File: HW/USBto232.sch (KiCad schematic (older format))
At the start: 17 parts

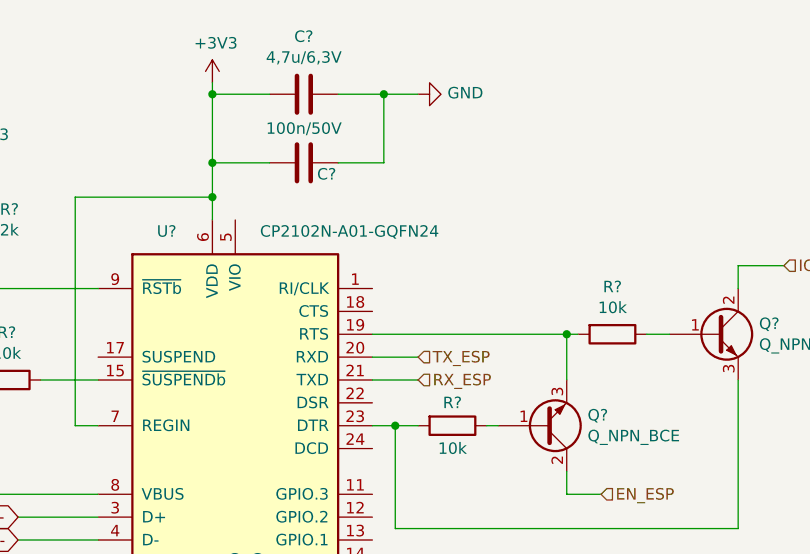
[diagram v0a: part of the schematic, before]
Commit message: add power supply for ESP, erase resistors by buttons, add power supply for CP2102, add communication control (CP2102-ESP)
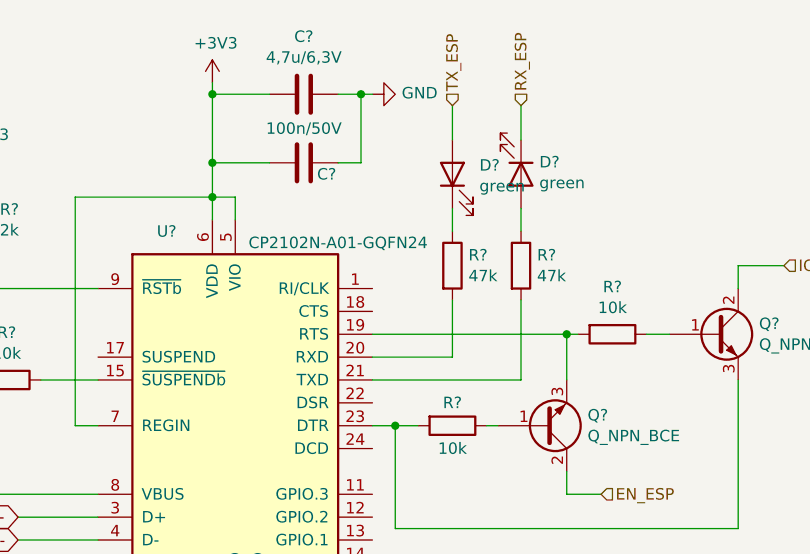
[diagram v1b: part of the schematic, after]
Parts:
- added D? (x2): green, symbol Device:LED
- added R? (x2): 47k, symbol Device:R
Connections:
- net +3V3: now also U?.5 (VIO)
- net RX_ESP: now also D?.1 (K); no longer U?.21 (TXD)
- net TX_ESP: now also D?.2 (A); no longer U?.20 (RXD)
- new net: D?.1 (K), R?.1
- new net: R?.2, U?.20 (RXD)
- new net: D?.2 (A), R?.1
- new net: R?.2, U?.21 (TXD)
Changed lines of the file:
@@
 $Descr A4 11693 8268
 encoding utf-8
-Sheet 6 9
+Sheet 13 16
 Title ""
 Date ""
@@
 Comment4 ""
 $EndDescr
-Wire Wire Line
-	6150 2800 6350 2800
-Wire Wire Line
-	6350 2900 6150 2900
 $Comp
 L Connector:USB_B_Micro J?
@@
 	1    0    0    -1
 $EndComp
-Text HLabel 6350 2800 2    50   Input ~ 0
+Text HLabel 6500 1700 1    50   Input ~ 0
 TX_ESP
-Text HLabel 6350 2900 2    50   Input ~ 0
+Text HLabel 6800 1700 1    50   Input ~ 0
 RX_ESP
 $Comp
@@
 	5450 1950 5450 2100
 Wire Wire Line
-	6000 1650 6200 1650
-Wire Wire Line
-	6200 1650 6200 1950
-Wire Wire Line
-	6200 1950 6000 1950
+	6000 1650 6100 1650
+Wire Wire Line
+	6100 1650 6100 1950
+Wire Wire Line
+	6100 1950 6000 1950
 $Comp
 L power:GND #PWR?
 U 1 1 5FBD8F58
-P 6350 1650
-F 0 "#PWR?" H 6350 1400 50  0001 C CNN
-F 1 "GND" V 6355 1522 50  0000 R CNN
-F 2 "" H 6350 1650 50  0001 C CNN
-F 3 "" H 6350 1650 50  0001 C CNN
-	1    6350 1650
+P 6150 1650
+F 0 "#PWR?" H 6150 1400 50  0001 C CNN
+F 1 "GND" V 6155 1522 50  0000 R CNN
+F 2 "" H 6150 1650 50  0001 C CNN
+F 3 "" H 6150 1650 50  0001 C CNN
+	1    6150 1650
 	0    -1   -1   0
 $EndComp
 Wire Wire Line
-	6350 1650 6200 1650
-Connection ~ 6200 1650
+	6150 1650 6100 1650
+Connection ~ 6100 1650
 $Comp
 L Device:R R?
@@
 AR Path="/5FBB3550/5FBB605D" Ref="U?"  Part="1"
 F 0 "U?" H 5250 3950 50  0000 C CNN
-F 1 "CP2102N-A01-GQFN24" H 6050 3950 50  0000 C CNN
+F 1 "CP2102N-A01-GQFN24" H 6000 3900 50  0000 C CNN
 F 2 "Package_DFN_QFN:QFN-24-1EP_4x4mm_P0.5mm_EP2.6x2.6mm" H 6000 2300 50  0001 L CNN
 F 3 "https://www.silabs.com/documents/public/data-sheets/cp2102n-datasheet.pdf" H 5600 2050 50  0001 C CNN
@@
 $EndComp
 NoConn ~ 1600 3050
+Wire Wire Line
+	5550 2200 5550 2100
+Wire Wire Line
+	5550 2100 5450 2100
+$Comp
+L Device:R R?
+U 1 1 5F7740AD
+P 6500 2400
+F 0 "R?" H 6570 2446 50  0000 L CNN
+F 1 "47k" H 6570 2355 50  0000 L CNN
+F 2 "" V 6430 2400 50  0001 C CNN
+F 3 "~" H 6500 2400 50  0001 C CNN
+	1    6500 2400
+	1    0    0    -1
+$EndComp
+$Comp
+L Device:R R?
+U 1 1 5F774323
+P 6800 2400
+F 0 "R?" H 6870 2446 50  0000 L CNN
+F 1 "47k" H 6870 2355 50  0000 L CNN
+F 2 "" V 6730 2400 50  0001 C CNN
+F 3 "~" H 6800 2400 50  0001 C CNN
+	1    6800 2400
+	1    0    0    -1
+$EndComp
+$Comp
+L Device:LED D?
+U 1 1 5F774688
+P 6500 2000
+F 0 "D?" V 6539 1882 50  0000 R CNN
+F 1 "green" V 6448 1882 50  0000 R CNN
+F 2 "" H 6500 2000 50  0001 C CNN
+F 3 "~" H 6500 2000 50  0001 C CNN
+	1    6500 2000
+	0    -1   -1   0
+$EndComp
+$Comp
+L Device:LED D?
+U 1 1 5F774C1B
+P 6800 2000
+F 0 "D?" V 6747 2080 50  0000 L CNN
+F 1 "green" V 6838 2080 50  0000 L CNN
+F 2 "" H 6800 2000 50  0001 C CNN
+F 3 "~" H 6800 2000 50  0001 C CNN
+	1    6800 2000
+	0    1    1    0
+$EndComp
+Wire Wire Line
+	6500 1700 6500 1850
+Wire Wire Line
+	6800 1700 6800 1850
+Wire Wire Line
+	6500 2150 6500 2250
+Wire Wire Line
+	6800 2150 6800 2250
+Wire Wire Line
+	6500 2550 6500 2800
+Wire Wire Line
+	6150 2800 6500 2800
+Wire Wire Line
+	6800 2900 6800 2550
+Wire Wire Line
+	6150 2900 6800 2900
 $EndSCHEMATC

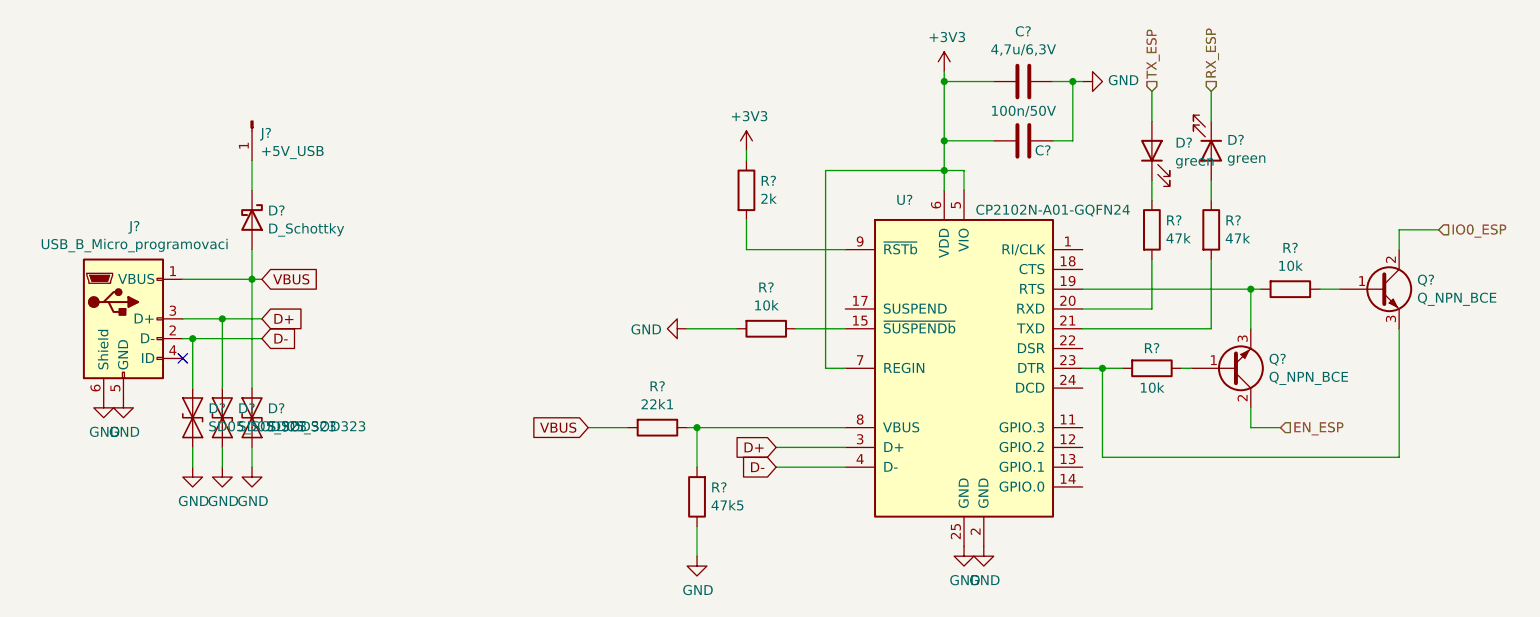
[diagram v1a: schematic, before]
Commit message: change USB
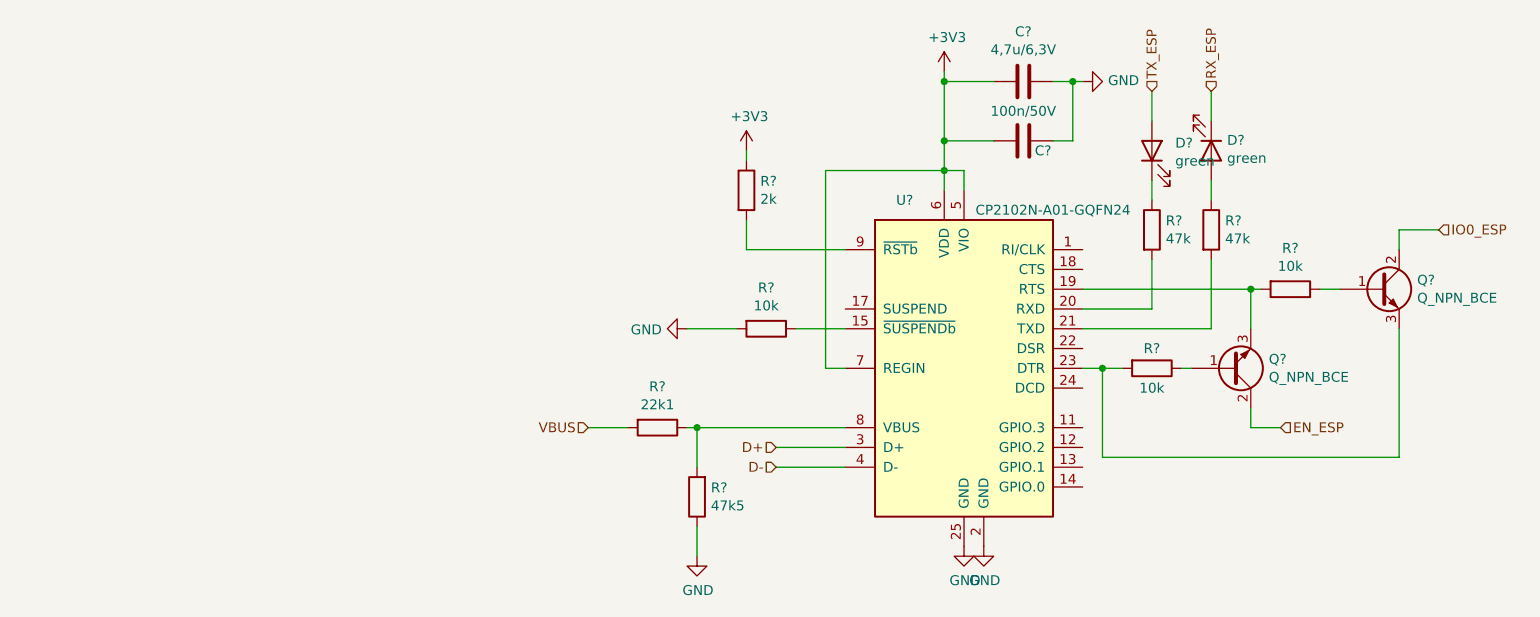
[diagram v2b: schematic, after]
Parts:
- removed D? (x3): SD05_SOD323, Diode_SMD:D_SOD-323, symbol Diode:SD05_SOD323
- removed D?: D_Schottky, symbol Device:D_Schottky
- removed J?: USB_B_Micro_programovaci, symbol Connector:USB_B_Micro
- removed J?: +5V_USB, symbol Connector:Conn_01x01_Male
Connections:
- no-connect marks 1 -> 0
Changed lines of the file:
@@
 $Descr A4 11693 8268
 encoding utf-8
-Sheet 13 16
+Sheet 13 17
 Title ""
 Date ""
@@
 Comment4 ""
 $EndDescr
-$Comp
-L Connector:USB_B_Micro J?
-U 1 1 5FBB6065
-P 1300 2850
-AR Path="/5FBB6065" Ref="J?"  Part="1"
-AR Path="/5FBB3550/5FBB6065" Ref="J?"  Part="1"
-F 0 "J?" H 1357 3317 50  0000 C CNN
-F 1 "USB_B_Micro_programovaci" H 1357 3226 50  0000 C CNN
-F 2 "" H 1450 2800 50  0001 C CNN
-F 3 "~" H 1450 2800 50  0001 C CNN
-	1    1300 2850
-	1    0    0    -1
-$EndComp
 Text HLabel 6500 1700 1    50   Input ~ 0
 TX_ESP
 Text HLabel 6800 1700 1    50   Input ~ 0
 RX_ESP
-$Comp
-L power:GND #PWR?
-U 1 1 5FBB7F58
-P 1300 3250
-F 0 "#PWR?" H 1300 3000 50  0001 C CNN
-F 1 "GND" H 1305 3077 50  0000 C CNN
-F 2 "" H 1300 3250 50  0001 C CNN
-F 3 "" H 1300 3250 50  0001 C CNN
-	1    1300 3250
-	1    0    0    -1
-$EndComp
 $Comp
 L power:GND #PWR?
@@
 Text HLabel 7950 2400 2    50   Input ~ 0
 IO0_ESP
-Text GLabel 4600 3500 0    50   Input ~ 0
-D+
-Text GLabel 4600 3600 0    50   Input ~ 0
-D-
-Text GLabel 2000 2850 2    50   Input ~ 0
-D+
-Text GLabel 2000 2950 2    50   Input ~ 0
-D-
-Wire Wire Line
-	2000 2850 1800 2850
-Wire Wire Line
-	1600 2950 1650 2950
 Wire Wire Line
 	4450 2500 4950 2500
@@
 Wire Wire Line
 	4200 3900 4200 4050
-Text GLabel 3650 3400 0    50   Input ~ 0
-VBUS
-Text GLabel 2000 2650 2    50   Input ~ 0
-VBUS
-Wire Wire Line
-	1600 2650 1950 2650
 $Comp
 L Interface_USB:CP2102N-A01-GQFN24 U?
@@
 	1    0    0    -1
 $EndComp
-$Comp
-L Diode:SD05_SOD323 D?
-U 1 1 5FBE6FA9
-P 1650 3350
-F 0 "D?" V 1696 3271 50  0000 R CNN
-F 1 "SD05_SOD323" V 1605 3271 50  0000 R CNN
-F 2 "Diode_SMD:D_SOD-323" H 1650 3150 50  0001 C CNN
-F 3 "https://www.littelfuse.com/~/media/electronics/datasheets/tvs_diode_arrays/littelfuse_tvs_diode_array_sd_c_datasheet.pdf.pdf" H 1650 3350 50  0001 C CNN
-	1    1650 3350
-	0    -1   -1   0
-$EndComp
 Wire Wire Line
 	4600 3500 4950 3500
 Wire Wire Line
 	4600 3600 4950 3600
-$Comp
-L Diode:SD05_SOD323 D?
-U 1 1 5FBE7A9C
-P 1800 3350
-F 0 "D?" V 1846 3271 50  0000 R CNN
-F 1 "SD05_SOD323" V 1755 3271 50  0000 R CNN
-F 2 "Diode_SMD:D_SOD-323" H 1800 3150 50  0001 C CNN
-F 3 "https://www.littelfuse.com/~/media/electronics/datasheets/tvs_diode_arrays/littelfuse_tvs_diode_array_sd_c_datasheet.pdf.pdf" H 1800 3350 50  0001 C CNN
-	1    1800 3350
-	0    -1   -1   0
-$EndComp
-$Comp
-L Diode:SD05_SOD323 D?
-U 1 1 5FBE7EF8
-P 1950 3350
-F 0 "D?" V 1996 3271 50  0000 R CNN
-F 1 "SD05_SOD323" V 1905 3271 50  0000 R CNN
-F 2 "Diode_SMD:D_SOD-323" H 1950 3150 50  0001 C CNN
-F 3 "https://www.littelfuse.com/~/media/electronics/datasheets/tvs_diode_arrays/littelfuse_tvs_diode_array_sd_c_datasheet.pdf.pdf" H 1950 3350 50  0001 C CNN
-	1    1950 3350
-	0    -1   -1   0
-$EndComp
-$Comp
-L power:GND #PWR?
-U 1 1 5FBE85DE
-P 1650 3600
-F 0 "#PWR?" H 1650 3350 50  0001 C CNN
-F 1 "GND" H 1655 3427 50  0000 C CNN
-F 2 "" H 1650 3600 50  0001 C CNN
-F 3 "" H 1650 3600 50  0001 C CNN
-	1    1650 3600
-	1    0    0    -1
-$EndComp
-$Comp
-L power:GND #PWR?
-U 1 1 5FBE8A8A
-P 1800 3600
-F 0 "#PWR?" H 1800 3350 50  0001 C CNN
-F 1 "GND" H 1805 3427 50  0000 C CNN
-F 2 "" H 1800 3600 50  0001 C CNN
-F 3 "" H 1800 3600 50  0001 C CNN
-	1    1800 3600
-	1    0    0    -1
-$EndComp
-$Comp
-L power:GND #PWR?
-U 1 1 5FBE8C03
-P 1950 3600
-F 0 "#PWR?" H 1950 3350 50  0001 C CNN
-F 1 "GND" H 1955 3427 50  0000 C CNN
-F 2 "" H 1950 3600 50  0001 C CNN
-F 3 "" H 1950 3600 50  0001 C CNN
-	1    1950 3600
-	1    0    0    -1
-$EndComp
-Wire Wire Line
-	1650 3500 1650 3600
-Wire Wire Line
-	1800 3500 1800 3600
-Wire Wire Line
-	1950 3500 1950 3600
-Wire Wire Line
-	1650 3200 1650 2950
-Connection ~ 1650 2950
-Wire Wire Line
-	1950 3200 1950 2650
-Connection ~ 1950 2650
-Wire Wire Line
-	1950 2650 2000 2650
-Wire Wire Line
-	1650 2950 2000 2950
-Wire Wire Line
-	1800 3200 1800 2850
-Connection ~ 1800 2850
-Wire Wire Line
-	1800 2850 1600 2850
-$Comp
-L Device:D_Schottky D?
-U 1 1 5FBF0650
-P 1950 2350
-F 0 "D?" V 1904 2430 50  0000 L CNN
-F 1 "D_Schottky" V 1995 2430 50  0000 L CNN
-F 2 "" H 1950 2350 50  0001 C CNN
-F 3 "~" H 1950 2350 50  0001 C CNN
-	1    1950 2350
-	0    1    1    0
-$EndComp
-Wire Wire Line
-	1950 2500 1950 2650
-$Comp
-L Connector:Conn_01x01_Male J?
-U 1 1 5FBF4956
-P 1950 1850
-F 0 "J?" V 2012 1894 50  0000 L CNN
-F 1 "+5V_USB" V 2103 1894 50  0000 L CNN
-F 2 "" H 1950 1850 50  0001 C CNN
-F 3 "~" H 1950 1850 50  0001 C CNN
-	1    1950 1850
-	0    1    1    0
-$EndComp
-Wire Wire Line
-	1950 2050 1950 2200
 Wire Wire Line
 	6650 3100 6700 3100
@@
 Wire Wire Line
 	3650 3400 3850 3400
-$Comp
-L power:GND #PWR?
-U 1 1 5F7442FA
-P 1200 3250
-F 0 "#PWR?" H 1200 3000 50  0001 C CNN
-F 1 "GND" H 1205 3077 50  0000 C CNN
-F 2 "" H 1200 3250 50  0001 C CNN
-F 3 "" H 1200 3250 50  0001 C CNN
-	1    1200 3250
-	1    0    0    -1
-$EndComp
-NoConn ~ 1600 3050
 Wire Wire Line
 	5550 2200 5550 2100
@@
 Wire Wire Line
 	6150 2900 6800 2900
+Text HLabel 3650 3400 0    50   Input ~ 0
+VBUS
+Text HLabel 4600 3500 0    50   Input ~ 0
+D+
+Text HLabel 4600 3600 0    50   Input ~ 0
+D-
 $EndSCHEMATC

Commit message: add some packages
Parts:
- C?: footprint (none) -> Capacitor_SMD:C_1206_3216Metric
- D? (x2): footprint (none) -> LED_SMD:LED_0603_1608Metric
- Q? (x2): footprint (none) -> Package_TO_SOT_SMD:SOT-23
- R? (x2): footprint (none) -> Resistor_SMD:R_0402_1005Metric
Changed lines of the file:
@@
 F 0 "Q?" H 7841 2746 50  0000 L CNN
 F 1 "Q_NPN_BCE" H 7841 2655 50  0000 L CNN
-F 2 "" H 7850 2800 50  0001 C CNN
+F 2 "Package_TO_SOT_SMD:SOT-23" H 7850 2800 50  0001 C CNN
 F 3 "~" H 7650 2700 50  0001 C CNN
 	1    7650 2700
@@
 F 0 "C?" V 5598 1650 50  0000 C CNN
 F 1 "4,7u/6,3V" V 5689 1650 50  0000 C CNN
-F 2 "" H 5888 1500 50  0001 C CNN
+F 2 "Capacitor_SMD:C_1206_3216Metric" H 5888 1500 50  0001 C CNN
 F 3 "~" H 5850 1650 50  0001 C CNN
 	1    5850 1650
@@
 F 0 "Q?" H 7091 3054 50  0000 L CNN
 F 1 "Q_NPN_BCE" H 7091 3145 50  0000 L CNN
-F 2 "" H 7100 3200 50  0001 C CNN
+F 2 "Package_TO_SOT_SMD:SOT-23" H 7100 3200 50  0001 C CNN
 F 3 "~" H 6900 3100 50  0001 C CNN
 	1    6900 3100
@@
 F 0 "R?" H 6570 2446 50  0000 L CNN
 F 1 "47k" H 6570 2355 50  0000 L CNN
-F 2 "" V 6430 2400 50  0001 C CNN
+F 2 "Resistor_SMD:R_0402_1005Metric" V 6430 2400 50  0001 C CNN
 F 3 "~" H 6500 2400 50  0001 C CNN
 	1    6500 2400
@@
 F 0 "R?" H 6870 2446 50  0000 L CNN
 F 1 "47k" H 6870 2355 50  0000 L CNN
-F 2 "" V 6730 2400 50  0001 C CNN
+F 2 "Resistor_SMD:R_0402_1005Metric" V 6730 2400 50  0001 C CNN
 F 3 "~" H 6800 2400 50  0001 C CNN
 	1    6800 2400
@@
 F 0 "D?" V 6539 1882 50  0000 R CNN
 F 1 "green" V 6448 1882 50  0000 R CNN
-F 2 "" H 6500 2000 50  0001 C CNN
+F 2 "LED_SMD:LED_0603_1608Metric" H 6500 2000 50  0001 C CNN
 F 3 "~" H 6500 2000 50  0001 C CNN
 	1    6500 2000
@@
 F 0 "D?" V 6747 2080 50  0000 L CNN
 F 1 "green" V 6838 2080 50  0000 L CNN
-F 2 "" H 6800 2000 50  0001 C CNN
+F 2 "LED_SMD:LED_0603_1608Metric" H 6800 2000 50  0001 C CNN
 F 3 "~" H 6800 2000 50  0001 C CNN
 	1    6800 2000

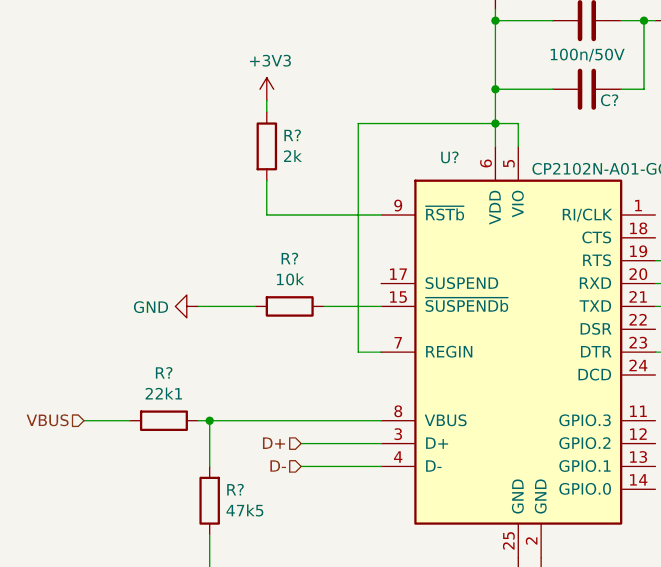
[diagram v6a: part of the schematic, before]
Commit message: add polyfuse for battery, remove resistor by SY8105, fix mistake by charger
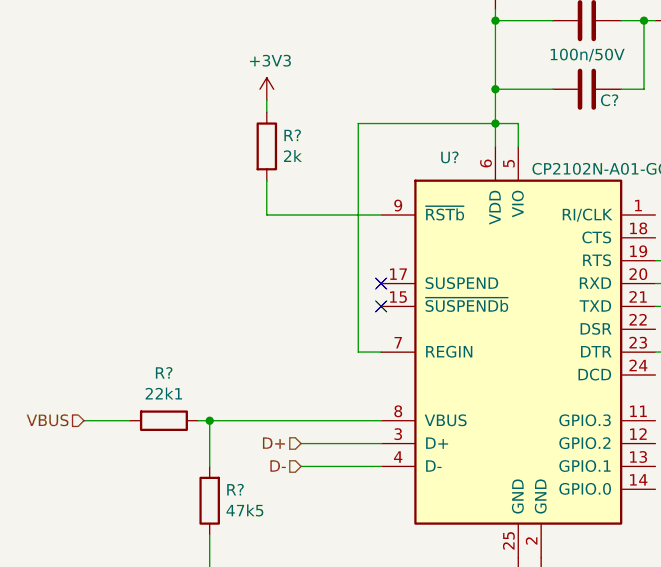
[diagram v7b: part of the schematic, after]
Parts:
- removed R?: 10k, Resistor_SMD:R_0402_1005Metric, symbol Device:R
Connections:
- no-connect marks 0 -> 2
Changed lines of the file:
@@
-$Comp
-L Device:R R?
-U 1 1 5FBDBF1A
-P 4550 2900
-F 0 "R?" V 4343 2900 50  0000 C CNN
-F 1 "10k" V 4434 2900 50  0000 C CNN
-F 2 "Resistor_SMD:R_0402_1005Metric" V 4480 2900 50  0001 C CNN
-F 3 "~" H 4550 2900 50  0001 C CNN
-	1    4550 2900
-	0    1    1    0
-$EndComp
-$Comp
-L power:GND #PWR?
-U 1 1 5FBDC504
-P 4150 2900
-F 0 "#PWR?" H 4150 2650 50  0001 C CNN
-F 1 "GND" V 4155 2772 50  0000 R CNN
-F 2 "" H 4150 2900 50  0001 C CNN
-F 3 "" H 4150 2900 50  0001 C CNN
-	1    4150 2900
-	0    1    1    0
-$EndComp
-Wire Wire Line
-	4150 2900 4400 2900
-Wire Wire Line
-	4700 2900 4950 2900
 $Comp
 L Device:R R?
@@
 Text HLabel 4600 3600 0    50   Input ~ 0
 D-
+NoConn ~ 4950 2900
+NoConn ~ 4950 2800
 $EndSCHEMATC
